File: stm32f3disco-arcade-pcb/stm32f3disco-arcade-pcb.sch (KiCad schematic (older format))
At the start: 28 parts, among them J1 STM32F3DISCO_P1, J10 NEOPIXEL3, J11 NEOPIXEL4, J12 BARREL_JACK, J13 I2C, J14 I2C, J2 STM32F3DISCO_P2, J3 GAMEPAD1, J4 GAMEPAD2, J5 GAMEPAD3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

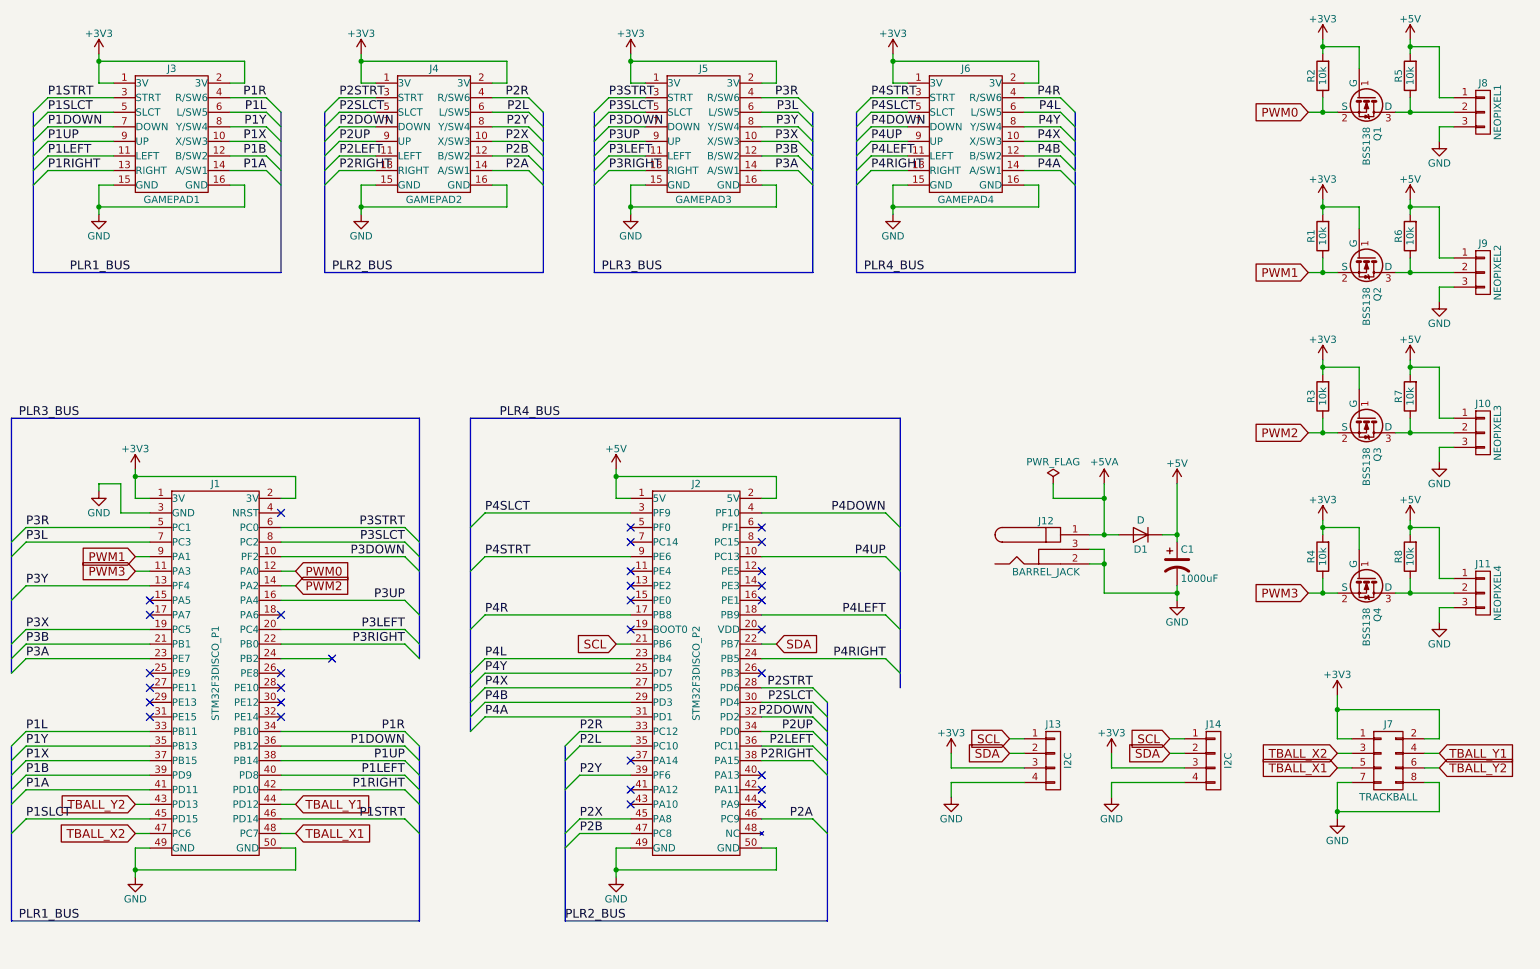
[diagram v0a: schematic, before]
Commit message: Fix UART pin assignment for STM32F3-Discovery
The STM32F3 Discovery user manual incorrectly says that USART1 is mapped
to PA9/10. It is not. It is mapped to PC4/5 instead, which requires a
change to the board design so that USART console output can be used.

Signed-off-by: Grant Likely <grant.likely@secretlab.ca>
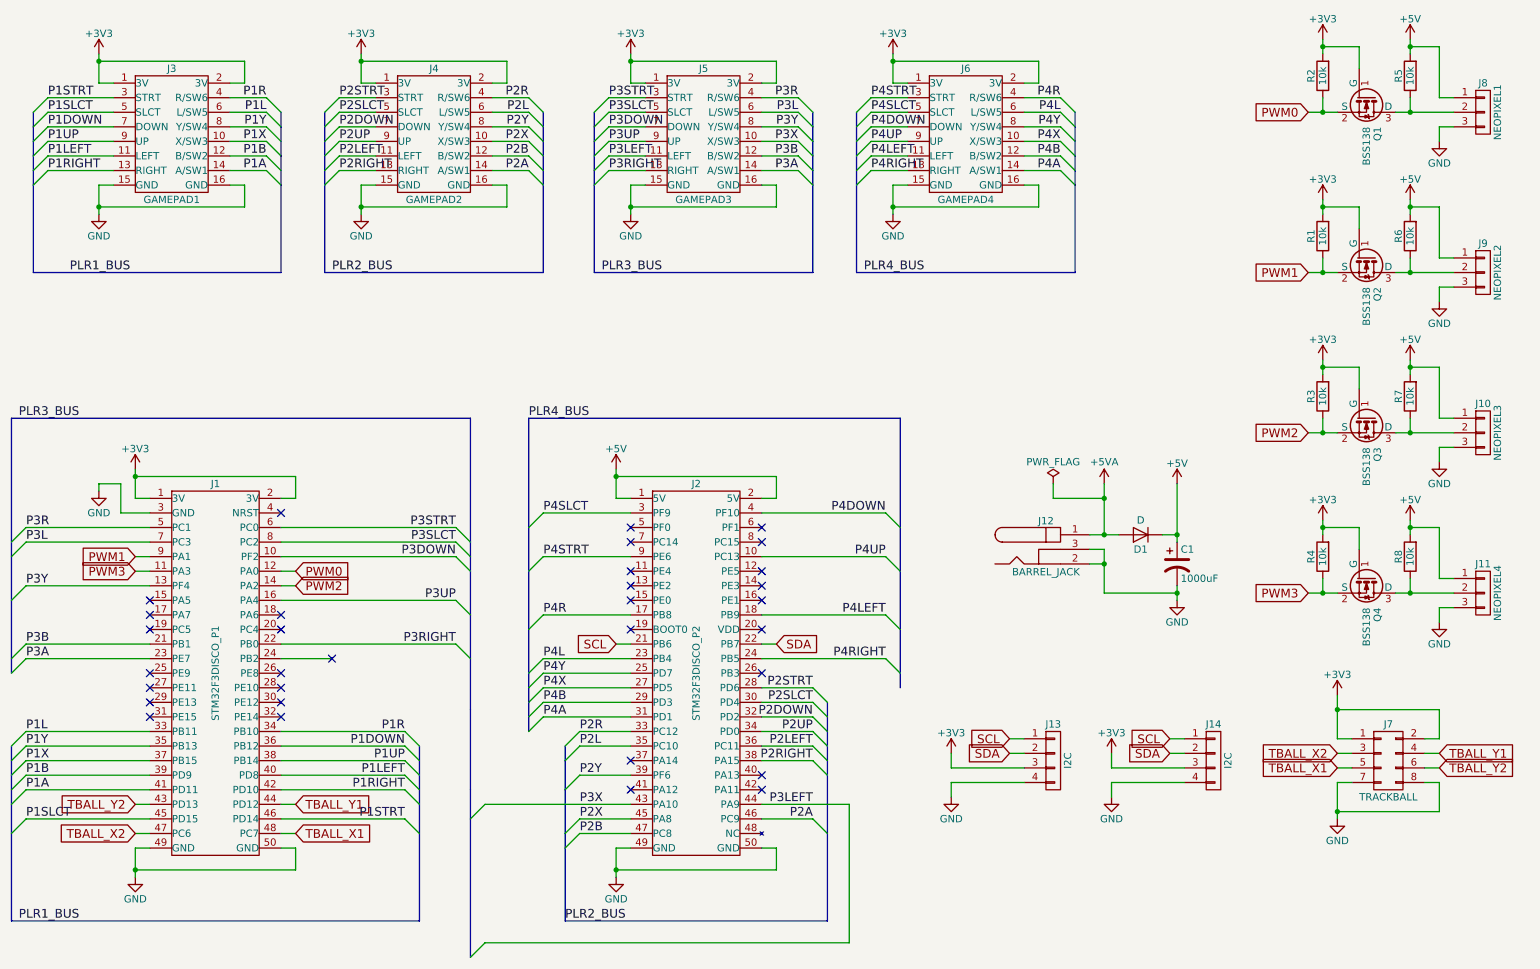
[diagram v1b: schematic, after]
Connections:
- net P3LEFT: now also J2.44 (PA9); no longer J1.20 (PC4)
- net P3X: now also J2.43 (PA10); no longer J1.19 (PC5)
